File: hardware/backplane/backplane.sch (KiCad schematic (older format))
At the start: 85 parts, among them J1 C96ABC, J10 Conn_Coaxial_Power, J2 C96ABC, J3 C96ABC, J4 C96ABC, J5 C96ABC, J6 C96ABC, J7 C96ABC, J8 C96ABC, J9 C96ABC, SW1 SW_Push, SW2 SW_SPDT, SW3 SW_SPDT, U1 74AHC14, U10 U13, U2 74AHC08, U4 74HC00, U7 NE556, U9 74AHCT125, X1 CXO_DIP8

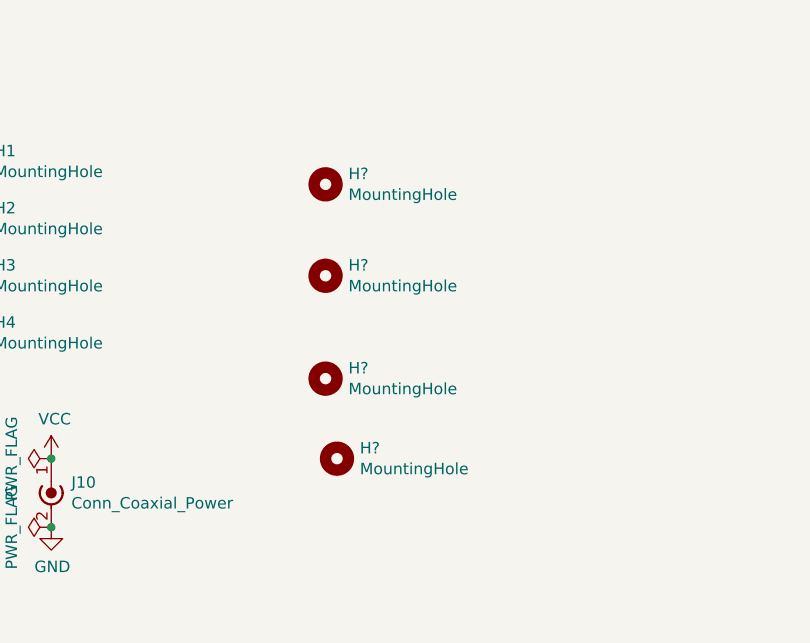
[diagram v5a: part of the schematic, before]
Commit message: backplane: change some parts to SMD (WIP)
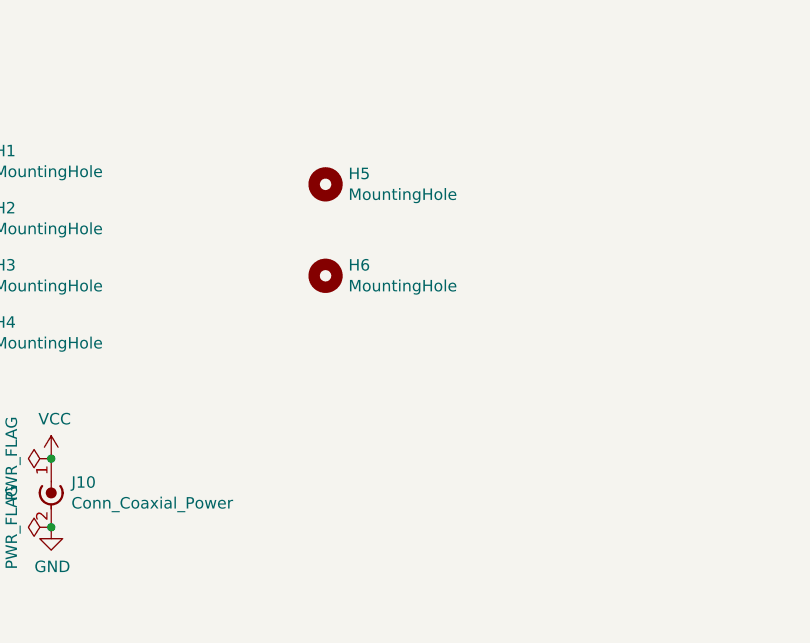
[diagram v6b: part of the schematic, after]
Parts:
- removed H? (x2): MountingHole, rails:7mm, symbol Mechanical:MountingHole
- CB2, CBU1, CBU2, CBU3, CBU4, CBX1: footprint Capacitor_THT:C_Rect_L7.0mm_W3.5mm_P5.00mm -> Capacitor_SMD:C_0805_2012Metric_Pad1.18x1.45mm_HandSolder
- R1, R10, R11, R2, R4, R6, R7, R8, R9: footprint Resistor_THT:R_Axial_DIN0207_L6.3mm_D2.5mm_P2.54mm_Vertical -> Resistor_SMD:R_0805_2012Metric_Pad1.20x1.40mm_HandSolder
- U7: footprint Package_DIP:DIP-14_W7.62mm_Socket -> Package_SO:SOIC-14_3.9x8.7mm_P1.27mm
- gave numbers to parts that had none: 2
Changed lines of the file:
@@
 F 0 "R9" H 7220 1846 50  0000 L CNN
 F 1 "4.7k" H 7220 1755 50  0000 L CNN
-F 2 "Resistor_THT:R_Axial_DIN0207_L6.3mm_D2.5mm_P2.54mm_Vertical" V 7080 1800 50  0001 C CNN
+F 2 "Resistor_SMD:R_0805_2012Metric_Pad1.20x1.40mm_HandSolder" V 7080 1800 50  0001 C CNN
 F 3 "~" H 7150 1800 50  0001 C CNN
 	1    7150 1800
@@
 F 0 "CBX1" H -2035 1196 50  0000 L CNN
 F 1 "0.1μF" H -2035 1105 50  0000 L CNN
-F 2 "Capacitor_THT:C_Rect_L7.0mm_W3.5mm_P5.00mm" H -2112 1000 50  0001 C CNN
+F 2 "Capacitor_SMD:C_0805_2012Metric_Pad1.18x1.45mm_HandSolder" H -2112 1000 50  0001 C CNN
 F 3 "~" H -2150 1150 50  0001 C CNN
 	1    -2150 1150
@@
 F 0 "CBU4" H -3335 1146 50  0000 L CNN
 F 1 "0.1μF" H -3335 1055 50  0000 L CNN
-F 2 "Capacitor_THT:C_Rect_L7.0mm_W3.5mm_P5.00mm" H -3412 950 50  0001 C CNN
+F 2 "Capacitor_SMD:C_0805_2012Metric_Pad1.18x1.45mm_HandSolder" H -3412 950 50  0001 C CNN
 F 3 "~" H -3450 1100 50  0001 C CNN
 	1    -3450 1100
@@
 F 0 "CBU1" H -5335 1296 50  0000 L CNN
 F 1 "0.1μF" H -5335 1205 50  0000 L CNN
-F 2 "Capacitor_THT:C_Rect_L7.0mm_W3.5mm_P5.00mm" H -5412 1100 50  0001 C CNN
+F 2 "Capacitor_SMD:C_0805_2012Metric_Pad1.18x1.45mm_HandSolder" H -5412 1100 50  0001 C CNN
 F 3 "~" H -5450 1250 50  0001 C CNN
 	1    -5450 1250
@@
 F 0 "R6" H 4900 5250 50  0000 L CNN
 F 1 "1k" H 4900 5150 50  0000 L CNN
-F 2 "Resistor_THT:R_Axial_DIN0207_L6.3mm_D2.5mm_P2.54mm_Vertical" V 4980 5200 50  0001 C CNN
+F 2 "Resistor_SMD:R_0805_2012Metric_Pad1.20x1.40mm_HandSolder" V 4980 5200 50  0001 C CNN
 F 3 "~" H 5050 5200 50  0001 C CNN
 	1    5050 5200
@@
 F 0 "R7" H 5220 5246 50  0000 L CNN
 F 1 "1k" H 5220 5155 50  0000 L CNN
-F 2 "Resistor_THT:R_Axial_DIN0207_L6.3mm_D2.5mm_P2.54mm_Vertical" V 5080 5200 50  0001 C CNN
+F 2 "Resistor_SMD:R_0805_2012Metric_Pad1.20x1.40mm_HandSolder" V 5080 5200 50  0001 C CNN
 F 3 "~" H 5150 5200 50  0001 C CNN
 	1    5150 5200
@@
 F 0 "U7" H 4200 6331 50  0000 C CNN
 F 1 "NE556" H 4200 6240 50  0000 C CNN
-F 2 "Package_DIP:DIP-14_W7.62mm_Socket" H 4200 5750 50  0001 C CNN
+F 2 "Package_SO:SOIC-14_3.9x8.7mm_P1.27mm" H 4200 5750 50  0001 C CNN
 F 3 "http://www.ti.com/lit/ds/symlink/ne556.pdf" H 4200 5750 50  0001 C CNN
 	1    4200 5750
@@
 F 0 "CBU3" H -4735 1196 50  0000 L CNN
 F 1 "0.1μF" H -4735 1105 50  0000 L CNN
-F 2 "Capacitor_THT:C_Rect_L7.0mm_W3.5mm_P5.00mm" H -4812 1000 50  0001 C CNN
+F 2 "Capacitor_SMD:C_0805_2012Metric_Pad1.18x1.45mm_HandSolder" H -4812 1000 50  0001 C CNN
 F 3 "~" H -4850 1150 50  0001 C CNN
 	1    -4850 1150
@@
 F 0 "R11" H 6600 5400 50  0000 L CNN
 F 1 "1k" H 6600 5300 50  0000 L CNN
-F 2 "Resistor_THT:R_Axial_DIN0207_L6.3mm_D2.5mm_P2.54mm_Vertical" V 6680 5350 50  0001 C CNN
+F 2 "Resistor_SMD:R_0805_2012Metric_Pad1.20x1.40mm_HandSolder" V 6680 5350 50  0001 C CNN
 F 3 "~" H 6750 5350 50  0001 C CNN
 	1    6750 5350
@@
 F 0 "R10" H 6350 5400 50  0000 L CNN
 F 1 "1k" H 6350 5300 50  0000 L CNN
-F 2 "Resistor_THT:R_Axial_DIN0207_L6.3mm_D2.5mm_P2.54mm_Vertical" V 6430 5350 50  0001 C CNN
+F 2 "Resistor_SMD:R_0805_2012Metric_Pad1.20x1.40mm_HandSolder" V 6430 5350 50  0001 C CNN
 F 3 "~" H 6500 5350 50  0001 C CNN
 	1    6500 5350
@@
 F 0 "CBU2" H -7785 1146 50  0000 L CNN
 F 1 "0.1μF" H -7785 1055 50  0000 L CNN
-F 2 "Capacitor_THT:C_Rect_L7.0mm_W3.5mm_P5.00mm" H -7862 950 50  0001 C CNN
+F 2 "Capacitor_SMD:C_0805_2012Metric_Pad1.18x1.45mm_HandSolder" H -7862 950 50  0001 C CNN
 F 3 "~" H -7900 1100 50  0001 C CNN
 	1    -7900 1100
@@
 F 0 "R2" H 3620 1046 50  0000 L CNN
 F 1 "1M" H 3620 955 50  0000 L CNN
-F 2 "Resistor_THT:R_Axial_DIN0207_L6.3mm_D2.5mm_P2.54mm_Vertical" V 3480 1000 50  0001 C CNN
+F 2 "Resistor_SMD:R_0805_2012Metric_Pad1.20x1.40mm_HandSolder" V 3480 1000 50  0001 C CNN
 F 3 "~" H 3550 1000 50  0001 C CNN
 	1    3550 1000
@@
 F 0 "CB2" H -6358 1196 50  0000 L CNN
 F 1 "0.1μF" H -6358 1105 50  0000 L CNN
-F 2 "Capacitor_THT:C_Rect_L7.0mm_W3.5mm_P5.00mm" H -6450 1150 50  0001 C CNN
+F 2 "Capacitor_SMD:C_0805_2012Metric_Pad1.18x1.45mm_HandSolder" H -6450 1150 50  0001 C CNN
 F 3 "~" H -6450 1150 50  0001 C CNN
 	1    -6450 1150
@@
 F 0 "R1" V 2900 1300 50  0000 L CNN
 F 1 "4.7k" V 3000 1250 50  0000 L CNN
-F 2 "Resistor_THT:R_Axial_DIN0207_L6.3mm_D2.5mm_P2.54mm_Vertical" V 2930 1350 50  0001 C CNN
+F 2 "Resistor_SMD:R_0805_2012Metric_Pad1.20x1.40mm_HandSolder" V 2930 1350 50  0001 C CNN
 F 3 "~" H 3000 1350 50  0001 C CNN
 	1    3000 1350
@@
 F 0 "U7" H 2050 6281 50  0000 C CNN
 F 1 "NE556" H 2050 6190 50  0000 C CNN
-F 2 "Package_DIP:DIP-14_W7.62mm_Socket" H 2050 5700 50  0001 C CNN
+F 2 "Package_SO:SOIC-14_3.9x8.7mm_P1.27mm" H 2050 5700 50  0001 C CNN
 F 3 "http://www.ti.com/lit/ds/symlink/ne556.pdf" H 2050 5700 50  0001 C CNN
 	2    2050 5700
@@
 F 0 "R4" H 1570 5246 50  0000 L CNN
 F 1 "1k" H 1570 5155 50  0000 L CNN
-F 2 "Resistor_THT:R_Axial_DIN0207_L6.3mm_D2.5mm_P2.54mm_Vertical" V 1430 5200 50  0001 C CNN
+F 2 "Resistor_SMD:R_0805_2012Metric_Pad1.20x1.40mm_HandSolder" V 1430 5200 50  0001 C CNN
 F 3 "~" H 1500 5200 50  0001 C CNN
 	1    1500 5200
@@
 F 0 "R8" H 2600 5700 50  0000 L CNN
 F 1 "1k" H 2600 5600 50  0000 L CNN
-F 2 "Resistor_THT:R_Axial_DIN0207_L6.3mm_D2.5mm_P2.54mm_Vertical" V 2680 5650 50  0001 C CNN
+F 2 "Resistor_SMD:R_0805_2012Metric_Pad1.20x1.40mm_HandSolder" V 2680 5650 50  0001 C CNN
 F 3 "~" H 2750 5650 50  0001 C CNN
 	1    2750 5650
@@
 	-650 -2650 -700 -2650
 $Comp
-L Mechanical:MountingHole H?
+L Mechanical:MountingHole H5
 U 1 1 A242A775
 P 13700 4850
-F 0 "H?" H 13800 4896 50  0000 L CNN
+F 0 "H5" H 13800 4896 50  0000 L CNN
 F 1 "MountingHole" H 13800 4805 50  0000 L CNN
 F 2 "rails:7mm" H 13700 4850 50  0001 C CNN
@@
 $EndComp
 $Comp
-L Mechanical:MountingHole H?
+L Mechanical:MountingHole H6
 U 1 1 A2589AFB
 P 13700 5250
-F 0 "H?" H 13800 5296 50  0000 L CNN
+F 0 "H6" H 13800 5296 50  0000 L CNN
 F 1 "MountingHole" H 13800 5205 50  0000 L CNN
 F 2 "rails:7mm" H 13700 5250 50  0001 C CNN
@@
 	1    0    0    -1
 $EndComp
-$Comp
-L Mechanical:MountingHole H?
-U 1 1 A2589DC3
-P 13700 5700
-F 0 "H?" H 13800 5746 50  0000 L CNN
-F 1 "MountingHole" H 13800 5655 50  0000 L CNN
-F 2 "rails:7mm" H 13700 5700 50  0001 C CNN
-F 3 "~" H 13700 5700 50  0001 C CNN
-	1    13700 5700
-	1    0    0    -1
-$EndComp
-$Comp
-L Mechanical:MountingHole H?
-U 1 1 A2589F42
-P 13750 6050
-F 0 "H?" H 13850 6096 50  0000 L CNN
-F 1 "MountingHole" H 13850 6005 50  0000 L CNN
-F 2 "rails:7mm" H 13750 6050 50  0001 C CNN
-F 3 "~" H 13750 6050 50  0001 C CNN
-	1    13750 6050
-	1    0    0    -1
-$EndComp

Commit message: backplane: use mostly SMD parts
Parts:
- removed D1, D2: DIODE, Diode_THT:D_DO-15_P2.54mm_Vertical_AnodeUp, symbol pspice:DIODE
- added CBU5, CBU6, CBU7: 0.1μF, Capacitor_SMD:C_0805_2012Metric_Pad1.18x1.45mm_HandSolder, symbol Device:C
- added D3: D_Schottky_x2_KCom_AAK, Package_TO_SOT_SMD:SOT-23_Handsoldering, symbol Device:D_Schottky_x2_KCom_AAK
- added U3, U5: 74AHC74, Package_SO:SOIC-14_3.9x8.7mm_P1.27mm, symbol 74xx:74LS74
- added U6: 74AHC02, Package_SO:SOIC-14_3.9x8.7mm_P1.27mm, symbol 74xx:74LS02
- C1, C2, C3, C4, CR1, CR2: footprint Capacitor_THT:C_Rect_L7.0mm_W3.5mm_P5.00mm -> Capacitor_SMD:C_0805_2012Metric_Pad1.18x1.45mm_HandSolder
- R3: footprint Resistor_THT:R_Axial_DIN0207_L6.3mm_D2.5mm_P2.54mm_Vertical -> Resistor_SMD:R_0805_2012Metric_Pad1.20x1.40mm_HandSolder
- U1, U2, U4, U9: footprint Package_DIP:DIP-14_W7.62mm_Socket -> Package_SO:SOIC-14_3.9x8.7mm_P1.27mm
- U10: value U13 -> 74HC00; footprint Package_DIP:DIP-14_W7.62mm_Socket -> Package_SO:SOIC-14_3.9x8.7mm_P1.27mm
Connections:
- net A27: now also U2.5, U6.2
- net A28: now also U1.3, U10.13
- net A31: now also U1.1, U10.9, U3.11 (C)
- net GND: now also CBU5.2, CBU6.2, CBU7.2, U3.7 (GND), U5.7 (GND), U6.11, U6.12, U6.5, U6.6, U6.7 (GND), U6.8, U6.9; no longer U1.1, U1.3, U10.10, U10.12, U10.13, U10.9, U2.4, U2.5, U4.12, U4.13
- net VCC: now also CBU5.1, CBU6.1, CBU7.1, U3.10 (~S), U3.14 (VCC), U3.4 (~S), U5.10 (~S), U5.14 (VCC), U5.4 (~S), U6.14 (VCC)
- net ~CLK_RST~: now also U3.1 (~R), U3.13 (~R), U5.1 (~R), U5.13 (~R)
- net ~RST_HDR~: now also D3.3 (K)
- net at U1.2: now also U3.3 (C)
- net at U1.4: now also U5.3 (C)
- net at U2.6: now also U5.2 (D)
- net at CR1.1, R2.2, U1.5: now also D3.1 (A)
- net at CR2.1, R3.2, U1.13: now also D3.2 (A)
- net at U10.8: now also U4.12
- net at U10.11: now also U4.13
- net PHI_2: now reaches U4.11
- new net: U2.4, U3.8 (~Q)
- new net: U10.10, U3.9 (Q)
- new net: U10.12, U5.9 (Q), U6.3
- new net: U3.2 (D), U6.1
- new net: U3.12 (D), U3.5 (Q)
- new net: U5.12 (D), U5.5 (Q)
- no-connect marks 72 -> 69
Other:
- note added: "TODO: put PHI_2 on the bus\nMaybe put it at A28 and move BASE_CLK to A31 to replace ~RST_HDR~"
- moved on the sheet: CBU2, CR2, JPC1, R1, R3, U10C, U10D, U1A, U1B, U1E, U1F, U2A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

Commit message: backplane: place traces
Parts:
- removed CBU4: 0.1μF, Capacitor_SMD:C_0805_2012Metric_Pad1.18x1.45mm_HandSolder, symbol Device:C
- removed R9: 4.7k, Resistor_SMD:R_0805_2012Metric_Pad1.20x1.40mm_HandSolder, symbol Device:R
- removed U9: 74AHCT125, Package_SO:SOIC-14_3.9x8.7mm_P1.27mm, symbol 74xx:74LS125
- added CBU7, CBU8: 0.1μF, Capacitor_SMD:C_0805_2012Metric_Pad1.18x1.45mm_HandSolder, symbol Device:C
- added U8: 74HC00, Package_SO:SOIC-14_3.9x8.7mm_P1.27mm, symbol 74xx:74HC00
- R1: value 4.7k -> 1k
- renumbered CBU3 to CBU10, CB2 to CBU2, CBU5 to CBU3, CBU2 to CBU4, CBU6 to CBU5, CBU7 to CBU6
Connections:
- net 555_AST: now also U10.9; no longer U4.2
- net 555_MONO: now also U10.13; no longer U4.5
- net A28: now also U4.6, U8.5; no longer U10.13, U2.11
- net A31: now also U8.1; no longer U10.9
- net GND: now also U2.12, U2.13, U4.12, U4.13, CBU7.2, CBU8.2, U8.12, U8.13, U8.7 (GND); no longer JP1.1
- net PHI_2: now also U8.8; no longer U4.11
- net SEL_AST: now also U10.10; no longer U4.1
- net SEL_MONO: now also U10.12; no longer U4.4
- net VCC: now also CBU7.1, CBU8.1, U8.14 (VCC)
- net ~CLK_RST~: now also U4.2; no longer U2.13
- net at SW2.2 (B): now also JP1.1
- net at CR1.1, R2.2, U1.5: now also D3.2 (A); no longer D3.1 (A)
- net at CR2.1, R3.2, U1.13: now also D3.1 (A); no longer D3.2 (A)
- net at U3.9 (Q): now also U8.2; no longer U10.10
- net at U10.8: now also U4.9; no longer U4.12
- net at U10.11: now also U4.10; no longer U4.13
- net at U5.9 (Q), U6.3: now also U8.4; no longer U10.12
- net at U4.3: now also U4.4, U4.5; no longer U4.9
- net ~CLK_ENABLE~: no longer names the net of JP1.2
- net ~CLK_ENABLE~: now also U4.1
- new net: U8.10, U8.6
- new net: U8.3, U8.9
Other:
- moved on the sheet: C1, C2, C3, C4, CBU1, CBU10, CBU2, CBU3, CBU4, CBU5, CBU6, CBX1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
